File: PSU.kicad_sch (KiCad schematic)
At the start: 6 parts, among them T1 AO3401

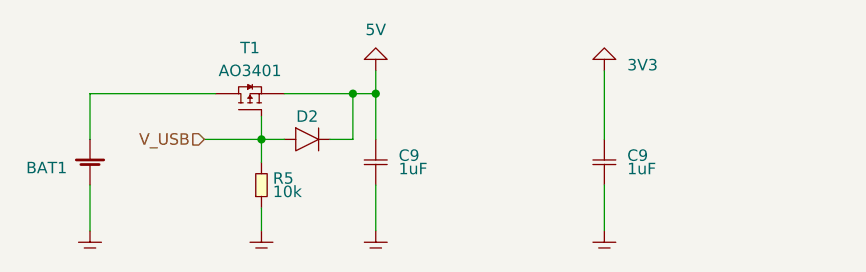
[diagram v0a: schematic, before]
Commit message: added usb serial and mcu
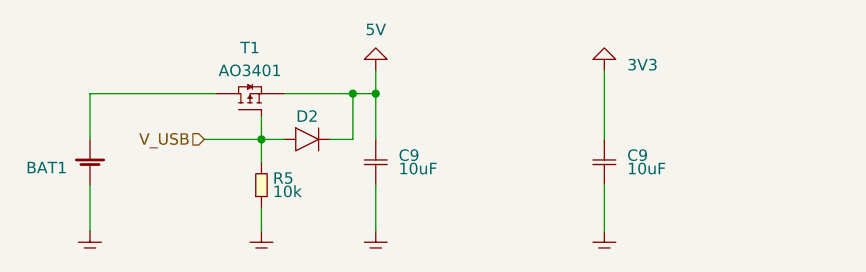
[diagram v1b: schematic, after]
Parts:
- C9: value 1uF -> 10uF
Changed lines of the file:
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@@
       (effects (font (size 1.27 1.27)) (justify left bottom))
     )
-    (property "Value" "1uF" (at 180.34 96.52 0)
+    (property "Value" "10uF" (at 180.34 96.52 0)
       (effects (font (size 1.27 1.27)) (justify left top))
     )
@@
       (effects (font (size 1.27 1.27)) (justify left bottom))
     )
-    (property "Value" "1uF" (at 154.94 96.52 0)
+    (property "Value" "10uF" (at 154.94 96.52 0)
       (effects (font (size 1.27 1.27)) (justify left top))
     )

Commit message: cleaned up layout, added 3V3 regulator, changed NTC to connect to gnd instead of 3V3, added README
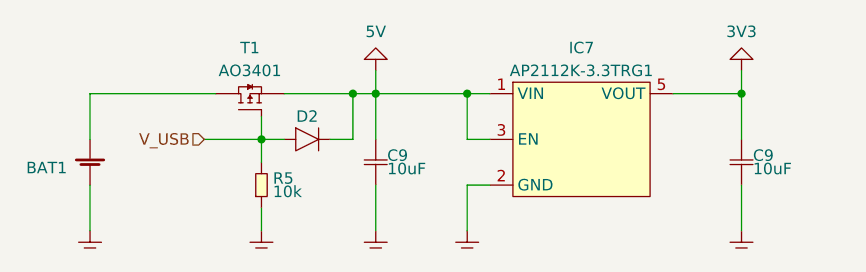
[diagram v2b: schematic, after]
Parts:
- added IC7: AP2112K-3.3TRG1, symbol Power:AP2112K-3.3TRG1
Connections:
- net GND: now also IC7.1 (VIN), IC7.2 (GND), IC7.3 (EN), IC7.5 (VOUT)
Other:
- moved on the sheet: C9
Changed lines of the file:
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@@
   (junction (at 149.86 88.9) (diameter 0) (color 0 0 0 0)
   )
+  (junction (at 162.56 88.9) (diameter 0) (color 0 0 0 0)
+  )
+  (junction (at 193.04 88.9) (diameter 0) (color 0 0 0 0)
+  )
   (junction (at 152.4 88.9) (diameter 0) (color 0 0 0 0)
   )
@@
     (stroke (width 0) (type default))
   )
-  (wire (pts (xy 177.8 99.06) (xy 177.8 104.14))
+  (wire (pts (xy 193.04 99.06) (xy 193.04 104.14))
     (stroke (width 0) (type default))
   )
@@
     (stroke (width 0) (type default))
   )
+  (wire (pts (xy 193.04 88.9) (xy 193.04 93.98))
+    (stroke (width 0) (type default))
+  )
+  (wire (pts (xy 162.56 104.14) (xy 162.56 99.06))
+    (stroke (width 0) (type default))
+  )
   (wire (pts (xy 120.65 99.06) (xy 120.65 104.14))
     (stroke (width 0) (type default))
@@
     (stroke (width 0) (type default))
   )
+  (wire (pts (xy 185.42 88.9) (xy 193.04 88.9))
+    (stroke (width 0) (type default))
+  )
+  (wire (pts (xy 162.56 99.06) (xy 165.1 99.06))
+    (stroke (width 0) (type default))
+  )
   (wire (pts (xy 139.7 96.52) (xy 139.7 93.98))
     (stroke (width 0) (type default))
   )
+  (wire (pts (xy 162.56 93.98) (xy 162.56 88.9))
+    (stroke (width 0) (type default))
+  )
   (wire (pts (xy 139.7 104.14) (xy 139.7 101.6))
     (stroke (width 0) (type default))
   )
+  (wire (pts (xy 152.4 88.9) (xy 162.56 88.9))
+    (stroke (width 0) (type default))
+  )
+  (wire (pts (xy 162.56 88.9) (xy 165.1 88.9))
+    (stroke (width 0) (type default))
+  )
+  (wire (pts (xy 165.1 93.98) (xy 162.56 93.98))
+    (stroke (width 0) (type default))
+  )
   (wire (pts (xy 133.35 93.98) (xy 139.7 93.98))
     (stroke (width 0) (type default))
@@
     (stroke (width 0) (type default))
   )
-  (wire (pts (xy 177.8 86.36) (xy 177.8 93.98))
+  (wire (pts (xy 193.04 86.36) (xy 193.04 88.9))
     (stroke (width 0) (type default))
   )
@@
       (effects (font (size 1.27 1.27)) hide)
     )
-    (property "Value" "5V" (at 152.4 82.55 0)
-      (effects (font (size 1.27 1.27)) (justify bottom))
+    (property "Value" "5V" (at 152.4 81.28 0)
+      (effects (font (size 1.27 1.27)) (justify top))
     )
     (property "Footprint" "" (at 152.4 86.36 0)
@@
     )
   )
-  (symbol (lib_id "generic:C") (at 177.8 96.52 0) (unit 1)
+  (symbol (lib_id "generic:C") (at 193.04 96.52 0) (unit 1)
     (in_bom yes) (on_board yes) (dnp no)
-    (property "Reference" "C9" (at 180.34 96.52 0)
+    (property "Reference" "C9" (at 194.31 96.52 0)
       (effects (font (size 1.27 1.27)) (justify left bottom))
     )
-    (property "Value" "10uF" (at 180.34 96.52 0)
+    (property "Value" "10uF" (at 194.31 96.52 0)
       (effects (font (size 1.27 1.27)) (justify left top))
     )
-    (property "Footprint" "SMT:0603" (at 177.8 99.06 0)
-      (effects (font (size 1.27 1.27)) hide)
-    )
-    (property "Datasheet" "" (at 177.8 96.52 0)
+    (property "Footprint" "SMT:0603" (at 193.04 99.06 0)
+      (effects (font (size 1.27 1.27)) hide)
+    )
+    (property "Datasheet" "" (at 193.04 96.52 0)
       (effects (font (size 1.27 1.27)) hide)
     )
@@
     )
   )
-  (symbol (lib_id "generic:3V3") (at 177.8 86.36 0) (unit 1)
-    (in_bom yes) (on_board yes) (dnp no) (fields_autoplaced)
-    (property "Reference" "3V01" (at 181.61 85.09 0)
-      (effects (font (size 1.27 1.27)) hide)
-    )
-    (property "Value" "3V3" (at 180.34 85.725 0)
-      (effects (font (size 1.27 1.27)) (justify left))
-    )
-    (property "Footprint" "" (at 177.8 86.36 0)
-      (effects (font (size 1.27 1.27)) hide)
-    )
-    (property "Datasheet" "" (at 177.8 86.36 0)
+  (symbol (lib_id "generic:3V3") (at 193.04 86.36 0) (unit 1)
+    (in_bom yes) (on_board yes) (dnp no)
+    (property "Reference" "3V01" (at 196.85 85.09 0)
+      (effects (font (size 1.27 1.27)) hide)
+    )
+    (property "Value" "3V3" (at 193.04 81.28 0)
+      (effects (font (size 1.27 1.27)) (justify top))
+    )
+    (property "Footprint" "" (at 193.04 86.36 0)
+      (effects (font (size 1.27 1.27)) hide)
+    )
+    (property "Datasheet" "" (at 193.04 86.36 0)
       (effects (font (size 1.27 1.27)) hide)
     )
@@
     )
   )
+  (symbol (lib_id "Power:AP2112K-3.3TRG1") (at 175.26 93.98 0) (unit 1)
+    (in_bom yes) (on_board yes) (dnp no) (fields_autoplaced)
+    (property "Reference" "IC7" (at 175.26 83.82 0)
+      (effects (font (size 1.27 1.27)))
+    )
+    (property "Value" "AP2112K-3.3TRG1" (at 175.26 86.36 0)
+      (effects (font (size 1.27 1.27)))
+    )
+    (property "Footprint" "" (at 172.72 93.98 0)
+      (effects (font (size 1.27 1.27)) hide)
+    )
+    (property "Datasheet" "https://www.diodes.com/assets/Datasheets/AP2112.pdf" (at 175.26 83.82 0)
+      (effects (font (size 1.27 1.27)) hide)
+    )
+    (property "MPN" "AP2112K-3.3TRG1" (at 175.26 86.36 0)
+      (effects (font (size 1.27 1.27)) hide)
+    )
+    (property "Digi-Key" "AP2112K-3.3TRG1DICT-ND" (at 172.72 101.6 0)
+      (effects (font (size 1.27 1.27)) hide)
+    )
+    (pin "1")
+    (pin "2")
+    (pin "3")
+    (pin "5")
+    (instances
+      (project "hikari"
+        (path "/020af8ab-593e-45b9-b2cd-8db025796961/88d27d54-d6a4-4c1b-84b3-09a59cbef514"
+          (reference "IC7") (unit 1)
+        )
+      )
+    )
+  )
   (symbol (lib_id "generic:GND") (at 152.4 104.14 0) (unit 1)
     (in_bom yes) (on_board yes) (dnp no) (fields_autoplaced)
@@
         (path "/020af8ab-593e-45b9-b2cd-8db025796961/88d27d54-d6a4-4c1b-84b3-09a59cbef514"
           (reference "GND04") (unit 1)
+        )
+      )
+    )
+  )
+  (symbol (lib_name "GND_1") (lib_id "generic:GND") (at 162.56 104.14 0) (unit 1)
+    (in_bom yes) (on_board yes) (dnp no) (fields_autoplaced)
+    (property "Reference" "GND021" (at 166.37 102.87 0)
+      (effects (font (size 1.27 1.27)) hide)
+    )
+    (property "Value" "GND" (at 166.37 104.14 0)
+      (effects (font (size 1.27 1.27)) hide)
+    )
+    (property "Footprint" "" (at 162.56 104.14 0)
+      (effects (font (size 1.27 1.27)) hide)
+    )
+    (property "Datasheet" "" (at 162.56 104.14 0)
+      (effects (font (size 1.27 1.27)) hide)
+    )
+    (pin "~")
+    (instances
+      (project "hikari"
+        (path "/020af8ab-593e-45b9-b2cd-8db025796961/88d27d54-d6a4-4c1b-84b3-09a59cbef514"
+          (reference "GND021") (unit 1)
         )
       )
@@
   (symbol (lib_id "generic:C") (at 152.4 96.52 0) (unit 1)
     (in_bom yes) (on_board yes) (dnp no)
-    (property "Reference" "C9" (at 154.94 96.52 0)
+    (property "Reference" "C9" (at 153.67 96.52 0)
       (effects (font (size 1.27 1.27)) (justify left bottom))
     )
-    (property "Value" "10uF" (at 154.94 96.52 0)
+    (property "Value" "10uF" (at 153.67 96.52 0)
       (effects (font (size 1.27 1.27)) (justify left top))
     )
@@
     )
   )
-  (symbol (lib_id "generic:GND") (at 177.8 104.14 0) (unit 1)
-    (in_bom yes) (on_board yes) (dnp no) (fields_autoplaced)
-    (property "Reference" "GND04" (at 181.61 102.87 0)
-      (effects (font (size 1.27 1.27)) hide)
-    )
-    (property "Value" "GND" (at 181.61 104.14 0)
-      (effects (font (size 1.27 1.27)) hide)
-    )
-    (property "Footprint" "" (at 177.8 104.14 0)
-      (effects (font (size 1.27 1.27)) hide)
-    )
-    (property "Datasheet" "" (at 177.8 104.14 0)
-      (effects (font (size 1.27 1.27)) hide)
-    )
+  (symbol (lib_id "generic:GND") (at 193.04 104.14 0) (unit 1)
+    (in_bom yes) (on_board yes) (dnp no) (fields_autoplaced)
+    (property "Reference" "GND04" (at 196.85 102.87 0)
+      (effects (font (size 1.27 1.27)) hide)
+    )
+    (property "Value" "GND" (at 196.85 104.14 0)
+      (effects (font (size 1.27 1.27)) hide)
+    )
+    (property "Footprint" "" (at 193.04 104.14 0)
+      (effects (font (size 1.27 1.27)) hide)
+    )
+    (property "Datasheet" "" (at 193.04 104.14 0)
+      (effects (font (size 1.27 1.27)) hide)
+    )

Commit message: fixed power symbols from showing up in BOM
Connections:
- net GND: no longer C9.1, D2.2 (K), IC7.1 (VIN), IC7.3 (EN), T1.2 (S)
- new net 5V: C9.1, D2.2 (K), IC7.1 (VIN), IC7.3 (EN), T1.2 (S)

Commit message: worked layout, fixed 3V3 being GND net
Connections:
- net GND: no longer C9.1, IC7.5 (VOUT)
- new net 3V3: C9.1, IC7.5 (VOUT)

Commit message: did most of todo items
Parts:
- BAT1: footprint (none) -> pin_headers:Battery_solder-points
- D2: value D -> SK22A; footprint SMT:0603 -> do:DO-214AC; symbol generic:D -> diodes:SK22A; Digi-Key (none) -> 4786-SK22ACT-ND
- IC7: footprint (none) -> SOT:SOT-23-5
- T1: value AO3401 -> GSF2301; symbol FET:AO3401 -> FET:GSF2301; Digi-Key (none) -> 4786-GSF2301CT-ND
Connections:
- net 5V: no longer IC7.3 (EN)
- new net Enable: IC7.3 (EN)
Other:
- moved on the sheet: C9, IC7

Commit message: added Digi-Key part numbers to BOM
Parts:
- C9: Digi-Key (none) -> 1276-1119-1-ND
- R5: Digi-Key (none) -> 13-RC0603JR-1010KLCT-ND
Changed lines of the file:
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@@
+      (effects (font (size 1.27 1.27)) hide)
+    )
+    (property "Digi-Key" "1276-1119-1-ND" (at 198.12 96.52 0)
       (effects (font (size 1.27 1.27)) hide)
     )
@@
       (effects (font (size 1.27 1.27)) hide)
     )
+    (property "Digi-Key" "13-RC0603JR-1010KLCT-ND" (at 139.7 99.06 0)
+      (effects (font (size 1.27 1.27)) hide)
+    )
     (pin "1")
     (pin "2")
@@
       (effects (font (size 1.27 1.27)) hide)
     )
+    (property "Digi-Key" "1276-1119-1-ND" (at 152.4 96.52 0)
+      (effects (font (size 1.27 1.27)) hide)
+    )
